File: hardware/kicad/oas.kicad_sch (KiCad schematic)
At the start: 0 parts

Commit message: kicad: split schematic into 4 hierarchical sheets (power/mcu/sensors/io)
Refactor from a single empty oas.kicad_sch into a hierarchical
schematic: root file referencing 4 empty sub-sheets, one per
PCB sector. Bumps SCH_VERSION to 20260306 (canonical KiCad
10.0.2). Adds deterministic UUIDs for both the (sheet ...)
blocks in root and the top-level UUID of each sub-sheet file.
Updates oas.kicad_pro sheets array to 5 entries.

ERC passes 0/0 across all five sheets. Two consecutive
regenerations produce a bit-identical diff (UUID determinism).

Sub-sheets currently empty - placeholder for upcoming
per-sector content (chunks #1b onward).

Co-Authored-By: Claude Opus 4.7 (1M context) <noreply@anthropic.com>
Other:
- added sheet IO (io.kicad_sch)
- added sheet MCU (mcu.kicad_sch)
- added sheet Power (power.kicad_sch)
- added sheet Sensors (sensors.kicad_sch)
- title: OAS — Open Ambient Sensor -> (none)
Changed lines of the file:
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@@
 (kicad_sch
-	(version 20260206)
+	(version 20260306)
 	(generator "eeschema")
 	(generator_version "10.0")
 	(paper "A4")
-	(title_block
-		(title "OAS — Open Ambient Sensor")
-		(date "2026-05-11")
-		(rev "0.1")
+(sheet
+	(at 50.8 50.8)
+	(size 38.1 12.7)
+	(exclude_from_sim no)
+	(in_bom yes)
+	(on_board yes)
+	(dnp no)
+	(fields_autoplaced yes)
+	(stroke
+		(width 0.1524)
+		(type solid)
 	)
-	(sheet_instances
-		(path "/" (page "1"))
+	(fill
+		(color 0 0 0 0.0000)
+	)
+	(property "Sheetname" "Power"
+		(at 50.8 50.0884 0)
+		(effects
+			(font
+				(size 1.27 1.27)
+			)
+			(justify left bottom)
+		)
+	)
+	(property "Sheetfile" "power.kicad_sch"
+		(at 50.8 63.9446 0)
+		(effects
+			(font
+				(size 1.27 1.27)
+			)
+			(justify left top)
+		)
+	)
+	(instances
+		(project "oas"
+			(path "/515343fe-5590-5fd9-97ec-5bed0f979de2"
+				(page "2")
+			)
+		)
 	)
 )
+(sheet
+	(at 101.6 50.8)
+	(size 38.1 12.7)
+	(exclude_from_sim no)
+	(in_bom yes)
+	(on_board yes)
+	(dnp no)
+	(fields_autoplaced yes)
+	(stroke
+		(width 0.1524)
+		(type solid)
+	)
+	(fill
+		(color 0 0 0 0.0000)
+	)
+	(property "Sheetname" "MCU"
+		(at 101.6 50.0884 0)
+		(effects
+			(font
+				(size 1.27 1.27)
+			)
+			(justify left bottom)
+		)
+	)
+	(property "Sheetfile" "mcu.kicad_sch"
+		(at 101.6 63.9446 0)
+		(effects
+			(font
+				(size 1.27 1.27)
+			)
+			(justify left top)
+		)
+	)
+	(instances
+		(project "oas"
+			(path "/515343fe-5590-5fd9-97ec-5bed0f979de2"
+				(page "3")
+			)
+		)
+	)
+)
+(sheet
+	(at 50.8 88.9)
+	(size 38.1 12.7)
+	(exclude_from_sim no)
+	(in_bom yes)
+	(on_board yes)
+	(dnp no)
+	(fields_autoplaced yes)
+	(stroke
+		(width 0.1524)
+		(type solid)
+	)
+	(fill
+		(color 0 0 0 0.0000)
+	)
+	(property "Sheetname" "Sensors"
+		(at 50.8 88.1884 0)
+		(effects
+			(font
+				(size 1.27 1.27)
+			)
+			(justify left bottom)
+		)
+	)
+	(property "Sheetfile" "sensors.kicad_sch"
+		(at 50.8 102.0446 0)
+		(effects
+			(font
+				(size 1.27 1.27)
+			)
+			(justify left top)
+		)
+	)
+	(instances
+		(project "oas"
+			(path "/515343fe-5590-5fd9-97ec-5bed0f979de2"
+				(page "4")
+			)
+		)
+	)
+)
+(sheet
+	(at 101.6 88.9)
+	(size 38.1 12.7)
+	(exclude_from_sim no)
+	(in_bom yes)
+	(on_board yes)
+	(dnp no)
+	(fields_autoplaced yes)
+	(stroke
+		(width 0.1524)
+		(type solid)
+	)
+	(fill
+		(color 0 0 0 0.0000)
+	)
+	(property "Sheetname" "IO"
+		(at 101.6 88.1884 0)
+		(effects
+			(font
+				(size 1.27 1.27)
+			)
+			(justify left bottom)
+		)
+	)
+	(property "Sheetfile" "io.kicad_sch"
+		(at 101.6 102.0446 0)
+		(effects
+			(font
+				(size 1.27 1.27)
+			)
+			(justify left top)
+		)
+	)
+	(instances
+		(project "oas"
+			(path "/515343fe-5590-5fd9-97ec-5bed0f979de2"
+				(page "5")
+			)
+		)
+	)
+)
+	(sheet_instances
+		(path "/"
+			(page "1")
+		)
+	)
+	(embedded_fonts no)
+)

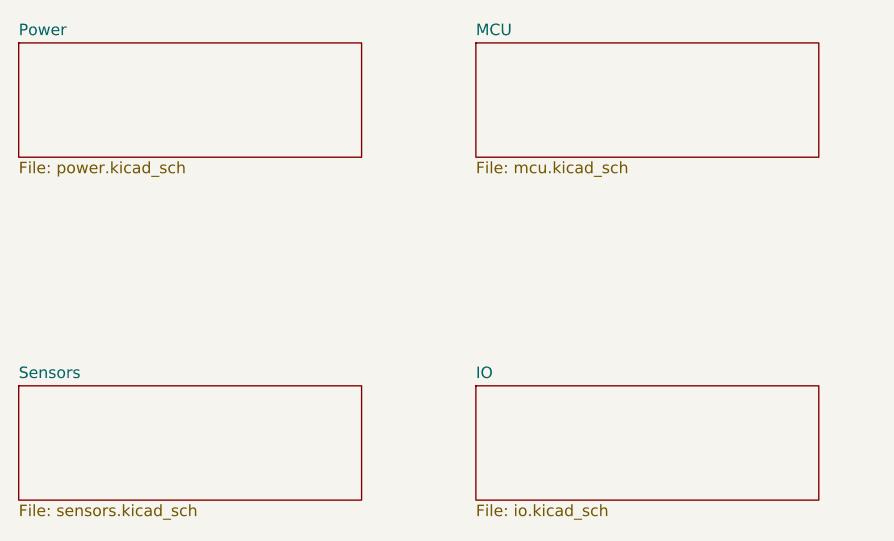
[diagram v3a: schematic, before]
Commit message: kicad: chunk #4 - MCU sub-sheet (ESP32-C6 SuperMini)
Populates mcu.kicad_sch with the ESP32-C6 SuperMini module
connector (U3), local 3.3V decoupling (C9 10uF + C9b 100nF),
and an unpopulated SWD/UART recovery header (J2, DNP).

ESP32-C6 SuperMini chosen per v0.3 research: lowest average
WiFi-active current (~60mA) thanks to WiFi 6 TWT/OFDMA, 512KB
SRAM headroom for BLE-proxy, ESPHome 2026 standardized on C6
for BLE-proxy roles. Antenna edge points to 12:00 (case wall)
per the clock-face sector layout.

Pinout (per v0.3 ARCHITECTURE.md, post strap-pin verification):
- GPIO 6 / 7: I2C SDA / SCL (shared bus, SEN66 + VEML7700 + NFC)
- GPIO 16 / 17: UART TX / RX (to LD2410 @ 256000 baud)
- GPIO 10: LD2410 OUT presence interrupt (was GPIO 4 - MTMS strap)
- GPIO 11: NFC FD interrupt (was GPIO 5 - MTDI strap)
- GPIO 8: onboard WS2812 status LED (no external WS2812 in v1)
- EN, GPIO 9: exposed on J2 recovery header

No external USB-C connector - flashing uses the SuperMini's own
onboard USB-C accessible before the enclosure is sealed. OTA via
ESPHome+HA handles all post-deployment updates.

J2 (SWD/UART recovery header, 6 pins) is marked DNP - footprint
exists on PCB for emergency hand-soldering if OTA fails, but is
not assembled by default.

Inter-sheet signals (I2C, UART, presence / NFC interrupts) are
exposed as hierarchical labels in mcu.kicad_sch and matching
sheet ports were preemptively added to oas.kicad_sch's MCU
sheet block, ready for the sensors sub-sheet (chunk #5).

Generator changes:
- New SUBSHEET_PINS dict + _gen_sheet_pin helper: declarative
  sheet port specification on the root sheet block.
- _gen_sheet_block rewritten without textwrap.dedent so the
  interpolated pin_block does not corrupt the leading whitespace
  pattern (fixes an indentation bug).
- _sch_capacitor and _sch_power_flag gained a sheet_key parameter
  (defaults to "power") so they can record the correct hierarchy
  path in their (instances ...) block when called from gen_mcu_sch.
- New hel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
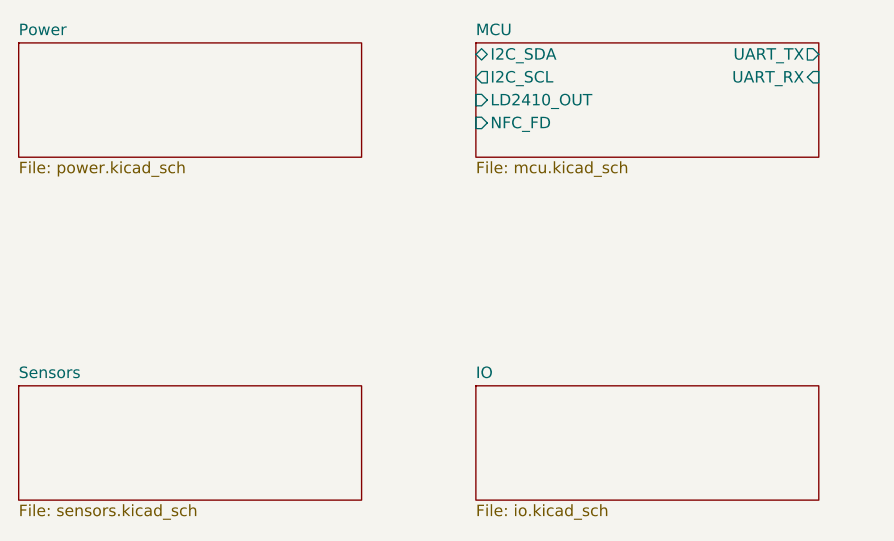
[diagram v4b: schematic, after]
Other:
- sheet MCU ports: added I2C_SCL, I2C_SDA, LD2410_OUT, NFC_FD, UART_RX, UART_TX; removed none

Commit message: kicad: chunk #5a - SEN66 reference footprint + 4 zip-tie NPTH + J3 socket
Adds the SEN66 (Sensirion SEN66-SIN-T, MPN 3.001.030, EAN N/A) connection
to the sensors sub-sheet and lays out the mechanical reference + retention
on the PCB. Resolves 2 of 6 expected ERC pin_not_connected (I2C_SDA, SCL).

Schematic (sensors.kicad_sch):
  J3 = JST GH 6-pin board socket (SM06B-GHS-TB compatible). Wiring per
  SEN6x datasheet Table 16: 1=VDD->+3V3, 2=GND, 3=SDA, 4=SCL,
  5=GND-redundant, 6=VDD-redundant (pins 5/6 internally tied to 1/2 in
  the SEN6x). Local 100 nF decoupling (C10) on the cable side of J3.

Custom PCB footprints:
  oas:SEN66_Mechanical_Reference - 55.2 x 25.6 mm body outline on F.Fab +
    F.SilkS, inlet/outlet markers at exact STEP-derived positions
    (inlet 1 obround at SEN66-local 10.7/7.4, inlet 2 rect at 10.65/18.85,
    outlet circle dia 20.74 at 42.4/12.8), connector marker on +X short
    edge, dashed sealing-divider hint at SEN66-local X=26. Mechanical-
    only, no pads (sensor is held by zip-ties, not soldered).
  oas:ZipTieHole_3mm_NPTH - reusable NPTH hole (3 mm drill, 4 mm silk
    ring, no copper) for ZT1..ZT4 mounting holes.

PCB placement (v0.7 of this chunk after user-iterated refinements):
  - SEN66 anchor at PCB (12, 25), rotation 90 CW. Body X 12..37.6,
    Y -30.2..25 -- clears all cutout zones (lowest cutout Y=27.2 at C2)
    by 2.2 mm. Long axis radial, connector edge at PCB top of body.
    Cross-sector placement (per user OK).
  - Zip-tie holes ZT1..ZT4 at SEN66-local (22, +-3) and (30, +-3).
    Both X positions in safe corridor [19.22, 31.03] so a 2 mm
    zip-tie band centred at each X passes over the SEN66 body
    without covering any inlet or outlet on the air-side face.
    PCB-global: ZT1=(9,3), ZT2=(40.6,3), ZT3=(9,-5), ZT4=(40.6,-5).
    All clear of cable pass-through hole (Phi 12) at origin.
  - J3 at PCB (48, 7), rotation 90 (vertical pin row, plug socket
    opening faces SEN66). 10.4 mm to body right edge for cable be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
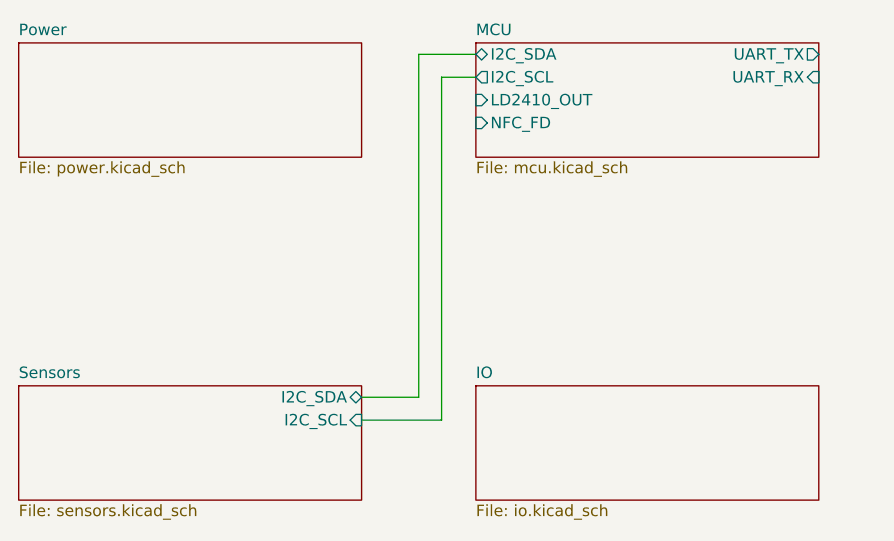
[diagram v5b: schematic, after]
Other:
- sheet Sensors ports: added I2C_SCL, I2C_SDA; removed none
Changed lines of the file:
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@@
+			)
+		)
+		(pin "I2C_SDA" bidirectional
+			(at 88.9 90.17 0)
+			(effects
+				(font
+					(size 1.27 1.27)
+				)
+				(justify left)
+			)
+		)
+		(pin "I2C_SCL" input
+			(at 88.9 92.71 0)
+			(effects
+				(font
+					(size 1.27 1.27)
+				)
+				(justify left)
 			)
 		)
@@
 		)
 	)
+(wire
+	(pts
+		(xy 88.9 90.17) (xy 95.25 90.17)
+	)
+	(stroke
+		(width 0)
+		(type default)
+	)
+)
+(wire
+	(pts
+		(xy 95.25 90.17) (xy 95.25 52.07)
+	)
+	(stroke
+		(width 0)
+		(type default)
+	)
+)
+(wire
+	(pts
+		(xy 95.25 52.07) (xy 101.6 52.07)
+	)
+	(stroke
+		(width 0)
+		(type default)
+	)
+)
+(wire
+	(pts
+		(xy 88.9 92.71) (xy 97.79 92.71)
+	)
+	(stroke
+		(width 0)
+		(type default)
+	)
+)
+(wire
+	(pts
+		(xy 97.79 92.71) (xy 97.79 54.61)
+	)
+	(stroke
+		(width 0)
+		(type default)
+	)
+)
+(wire
+	(pts
+		(xy 97.79 54.61) (xy 101.6 54.61)
+	)
+	(stroke
+		(width 0)
+		(type default)
+	)
+)
 	(sheet_instances
 		(path "/"

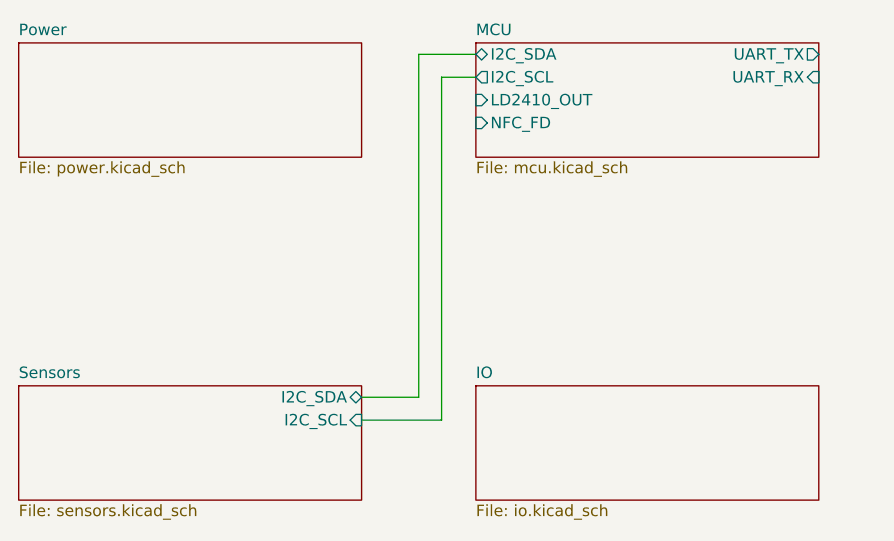
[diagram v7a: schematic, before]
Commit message: kicad: chunk #5b - LD2410 mmWave radar (J4 + C11) in sensors.kicad_sch
Adds the HLK-LD2410B presence radar connection to the sensors sub-sheet.
Resolves 4 of the 5 ERC issues that remained after chunk #5a:
- 3 sensors-side hier labels (LD2410_OUT, UART_TX, UART_RX) now exist
  and are wired through to the MCU side
- 3 root-sheet inter-sheet wires bind the matching sensors/mcu sheet
  pins so KiCad ERC sees the cross-sheet nets as electrically continuous

Schematic content (sensors.kicad_sch):
  J4 — JST SM05B-GHS-TB 5-pin board socket, mates with HLK-LD2410B
       stock cable. Pinout (per HiLink LD2410B datasheet):
         Pin 1: VCC (+5V from U1)
         Pin 2: GND
         Pin 3: TX  -> UART_RX (LD2410 output drives MCU GPIO 17)
         Pin 4: RX  <- UART_TX (MCU GPIO 16 drives LD2410 input)
         Pin 5: OUT -> LD2410_OUT (presence interrupt to MCU GPIO 2)
       Logic levels are 3.3 V TTL on TX/RX/OUT despite the 5 V supply,
       so the ESP32-C6 sees compatible levels without a level shifter.
  C11 — 100 nF 0402 X7R, local decoupling between +5V and GND at the
       J4 plug. Damps cable transient ringing on the +5V rail.

New schematic library symbols loaded verbatim from KiCad 10 stock libs
via the new `_read_kicad_lib_symbol()` helper (which prefixes the
symbol name with its library nickname and re-indents to fit our
embedded lib_symbols block):
  Connector_Generic:Conn_01x05
  power:+5V

New schematic helper:
  `_sch_conn_01x05()` — emits a 5-pin Conn_01x05 instance. Mirrors
  `_sch_conn_01x06` with one fewer pin and the Value property anchored
  at Y+10.16 (vs Y+12.7 for the 6-pin variant) to track the bottom
  pin's new Y position.

Root sheet (oas.kicad_sch) gains 3 new inter-sheet wire groups:
  - LD2410_OUT : sensors (88.9, 95.25) -> MCU left (101.6, 57.15) via
                 a vertical leg at X=100.33.
  - UART_TX    : sensors (88.9, 97.79) -> MCU right (139.7, 52.07) via
                 a vertical leg at X=143.51 (past the io block's east
 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
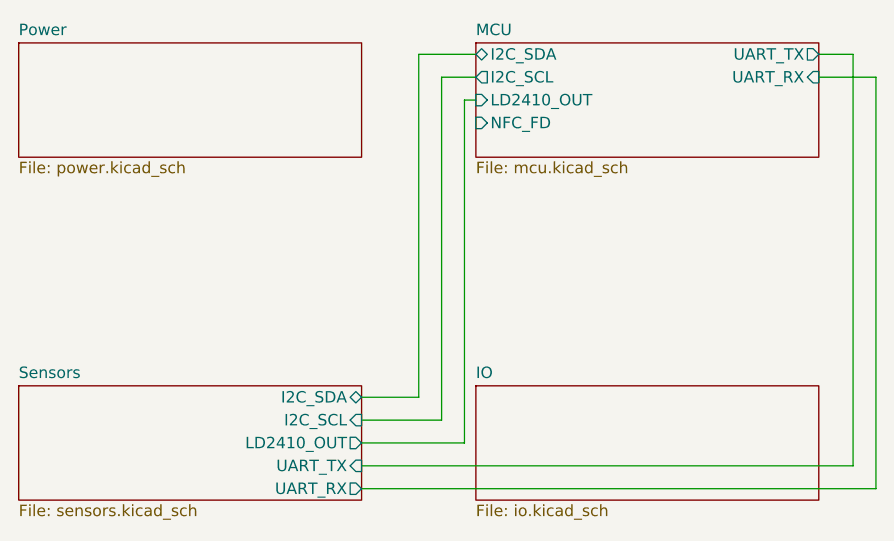
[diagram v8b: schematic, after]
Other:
- sheet Sensors ports: added LD2410_OUT, UART_RX, UART_TX; removed none
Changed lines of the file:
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@@
+			)
+		)
+		(pin "LD2410_OUT" output
+			(at 88.9 95.25 0)
+			(effects
+				(font
+					(size 1.27 1.27)
+				)
+				(justify left)
+			)
+		)
+		(pin "UART_TX" input
+			(at 88.9 97.79 0)
+			(effects
+				(font
+					(size 1.27 1.27)
+				)
+				(justify left)
+			)
+		)
+		(pin "UART_RX" output
+			(at 88.9 100.33 0)
+			(effects
+				(font
+					(size 1.27 1.27)
+				)
+				(justify left)
 			)
 		)
@@
 	)
 	(stroke
+		(width 0)
+		(type default)
+	)
+)
+(wire
+	(pts
+		(xy 88.9 95.25) (xy 100.33 95.25)
+	)
+	(stroke
+		(width 0)
+		(type default)
+	)
+)
+(wire
+	(pts
+		(xy 100.33 95.25) (xy 100.33 57.15)
+	)
+	(stroke
+		(width 0)
+		(type default)
+	)
+)
+(wire
+	(pts
+		(xy 100.33 57.15) (xy 101.6 57.15)
+	)
+	(stroke
+		(width 0)
+		(type default)
+	)
+)
+(wire
+	(pts
+		(xy 88.9 97.79) (xy 143.51 97.79)
+	)
+	(stroke
+		(width 0)
+		(type default)
+	)
+)
+(wire
+	(pts
+		(xy 143.51 97.79) (xy 143.51 52.07)
+	)
+	(stroke
+		(width 0)
+		(type default)
+	)
+)
+(wire
+	(pts
+		(xy 143.51 52.07) (xy 139.7 52.07)
+	)
+	(stroke
+		(width 0)
+		(type default)
+	)
+)
+(wire
+	(pts
+		(xy 88.9 100.33) (xy 146.05 100.33)
+	)
+	(stroke
+		(width 0)
+		(type default)
+	)
+)
+(wire
+	(pts
+		(xy 146.05 100.33) (xy 146.05 54.61)
+	)
+	(stroke
+		(width 0)
+		(type default)
+	)
+)
+(wire
+	(pts
+		(xy 146.05 54.61) (xy 139.7 54.61)
+	)
+	(stroke
